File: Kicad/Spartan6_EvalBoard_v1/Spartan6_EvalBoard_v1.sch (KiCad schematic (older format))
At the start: 0 parts

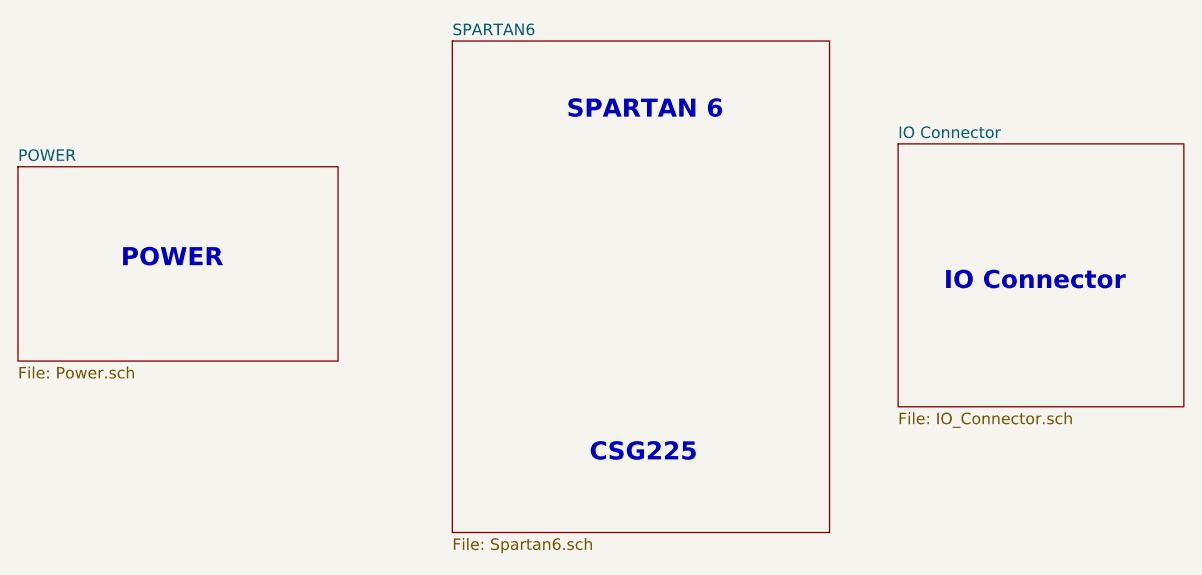
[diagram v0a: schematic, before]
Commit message: Schematic almost done
Schematic almost done, just to connect connector to FPGA
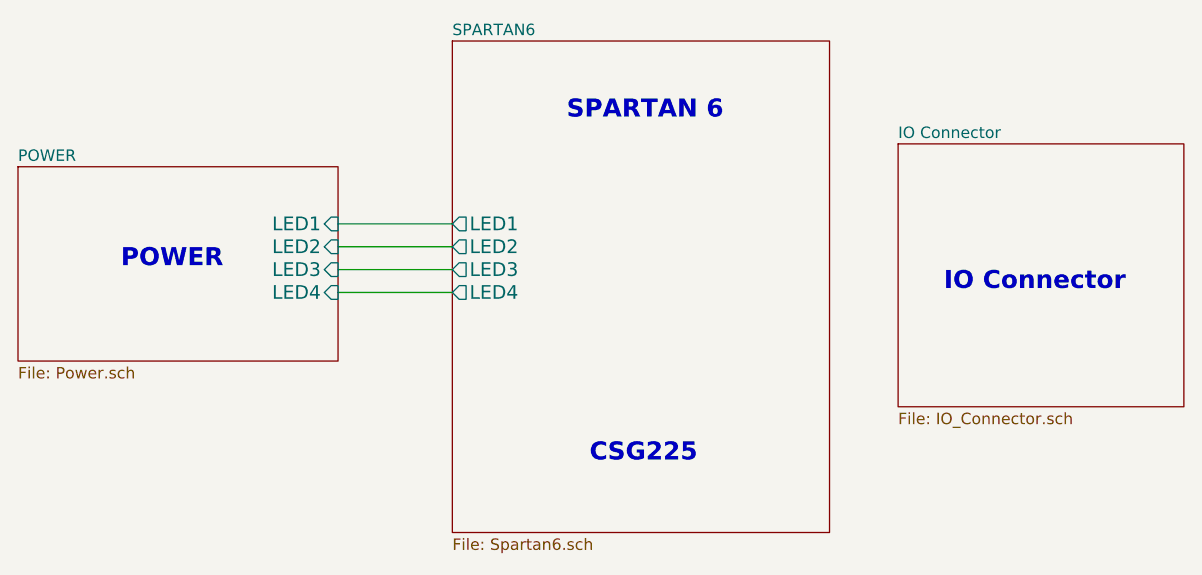
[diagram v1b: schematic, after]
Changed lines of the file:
@@
 LIBS:adc-dac
 LIBS:memory
-LIBS:xilinx
 LIBS:special
 LIBS:microcontrollers
@@
 LIBS:valves
 LIBS:numato_kicad_lib
+LIBS:xilinx
+LIBS:Eric
 LIBS:Spartan6_EvalBoard_v1-cache
 EELAYER 27 0
@@
 Sheet 1 4
 Title ""
-Date "26 sep 2014"
+Date "1 oct 2014"
 Rev ""
 Comp ""
@@
 F0 "POWER" 50
 F1 "Power.sch" 50
+F2 "LED1" I R 4500 3250 60
+F3 "LED2" I R 4500 3350 60
+F4 "LED3" I R 4500 3450 60
+F5 "LED4" I R 4500 3550 60
 $EndSheet
 Text Notes 3550 3450 0    79   ~ 16
@@
 F0 "SPARTAN6" 50
 F1 "Spartan6.sch" 50
+F2 "LED1" O L 5000 3250 60
+F3 "LED2" O L 5000 3350 60
+F4 "LED3" O L 5000 3450 60
+F5 "LED4" O L 5000 3550 60
 $EndSheet
 Text Notes 5600 4300 0    79   ~ 16
 CSG225
+Wire Wire Line
+	5000 3250 4500 3250
+Wire Wire Line
+	5000 3350 4500 3350
+Wire Wire Line
+	5000 3450 4500 3450
+Wire Wire Line
+	5000 3550 4500 3550
 $EndSCHEMATC

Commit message: Schematic and netllist created
The correct fpga connection to connector will have to be carried out.
Some more footprints need to be created.
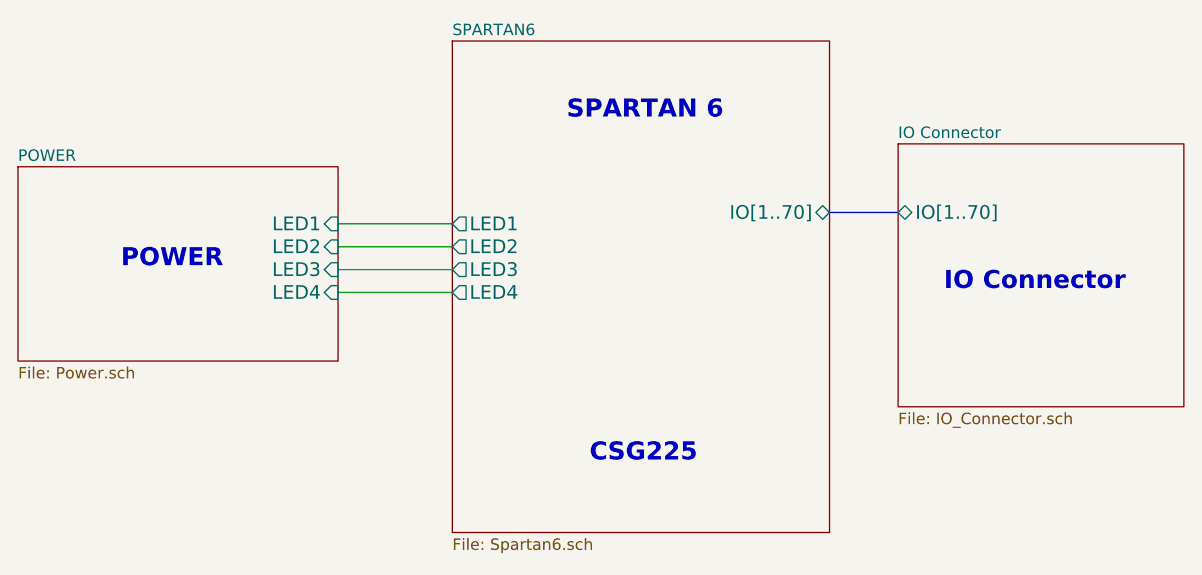
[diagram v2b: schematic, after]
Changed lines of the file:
@@
 Sheet 1 4
 Title ""
-Date "1 oct 2014"
+Date "2 oct 2014"
 Rev ""
 Comp ""
@@
 F0 "IO Connector" 50
 F1 "IO_Connector.sch" 50
+F2 "IO[1..70]" B L 6950 3200 60
 $EndSheet
 Text Notes 7150 3550 0    79   ~ 16
@@
 F4 "LED3" O L 5000 3450 60
 F5 "LED4" O L 5000 3550 60
+F6 "IO[1..70]" B R 6650 3200 60
 $EndSheet
 Text Notes 5600 4300 0    79   ~ 16
@@
 Wire Wire Line
 	5000 3550 4500 3550
+Wire Bus Line
+	6950 3200 6650 3200
 $EndSCHEMATC

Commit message: Schematic completed, layout starte
Schematic completed, layout starte
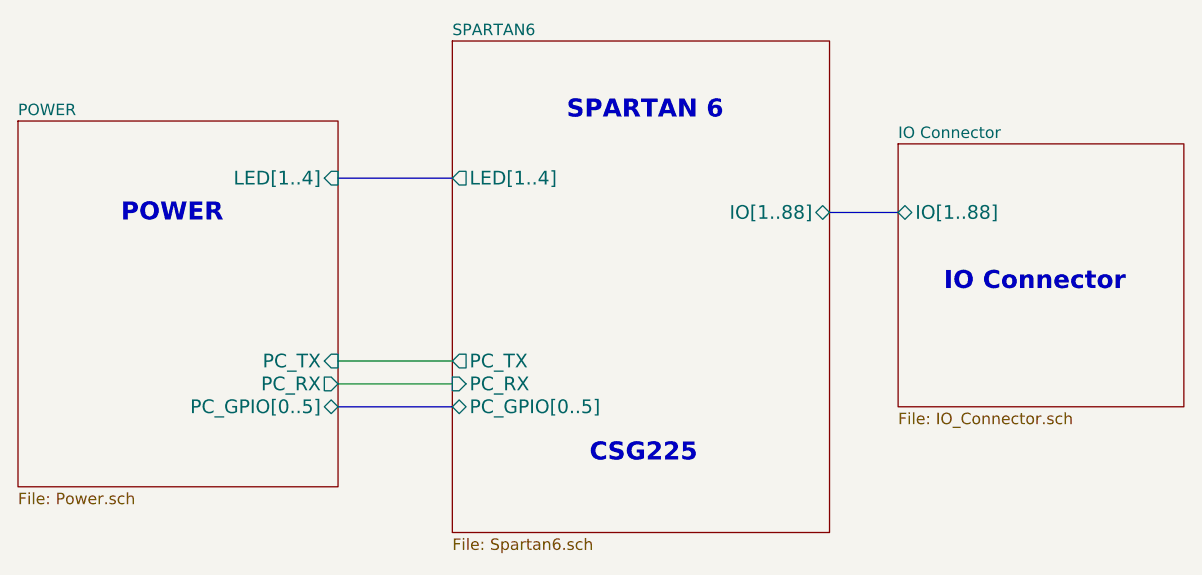
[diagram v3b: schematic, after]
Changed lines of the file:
@@
 Sheet 1 4
 Title ""
-Date "2 oct 2014"
+Date "22 oct 2014"
 Rev ""
 Comp ""
@@
 F0 "IO Connector" 50
 F1 "IO_Connector.sch" 50
-F2 "IO[1..70]" B L 6950 3200 60
+F2 "IO[1..88]" B L 6950 3200 60
 $EndSheet
 Text Notes 7150 3550 0    79   ~ 16
 IO Connector
+Text Notes 3550 3250 0    79   ~ 16
+POWER
+Text Notes 5600 4300 0    79   ~ 16
+CSG225
 $Sheet
-S 3100 3000 1400 850
+S 3100 2800 1400 1600
 U 5425C5A1
 F0 "POWER" 50
 F1 "Power.sch" 50
-F2 "LED1" I R 4500 3250 60
-F3 "LED2" I R 4500 3350 60
-F4 "LED3" I R 4500 3450 60
-F5 "LED4" I R 4500 3550 60
+F2 "LED[1..4]" I R 4500 3050 60
+F3 "PC_GPIO[0..5]" B R 4500 4050 60
+F4 "PC_TX" I R 4500 3850 60
+F5 "PC_RX" O R 4500 3950 60
 $EndSheet
-Text Notes 3550 3450 0    79   ~ 16
-POWER
+Wire Bus Line
+	6950 3200 6650 3200
+Wire Wire Line
+	5000 3850 4500 3850
+Wire Wire Line
+	4500 3950 5000 3950
+Wire Bus Line
+	4500 4050 5000 4050
 $Sheet
 S 5000 2450 1650 2150
@@
 F0 "SPARTAN6" 50
 F1 "Spartan6.sch" 50
-F2 "LED1" O L 5000 3250 60
-F3 "LED2" O L 5000 3350 60
-F4 "LED3" O L 5000 3450 60
-F5 "LED4" O L 5000 3550 60
-F6 "IO[1..70]" B R 6650 3200 60
+F2 "LED[1..4]" O L 5000 3050 60
+F3 "IO[1..88]" B R 6650 3200 60
+F4 "PC_GPIO[0..5]" B L 5000 4050 60
+F5 "PC_TX" O L 5000 3850 60
+F6 "PC_RX" I L 5000 3950 60
 $EndSheet
-Text Notes 5600 4300 0    79   ~ 16
-CSG225
-Wire Wire Line
-	5000 3250 4500 3250
-Wire Wire Line
-	5000 3350 4500 3350
-Wire Wire Line
-	5000 3450 4500 3450
-Wire Wire Line
-	5000 3550 4500 3550
 Wire Bus Line
-	6950 3200 6650 3200
+	5000 3050 4500 3050
 $EndSCHEMATC

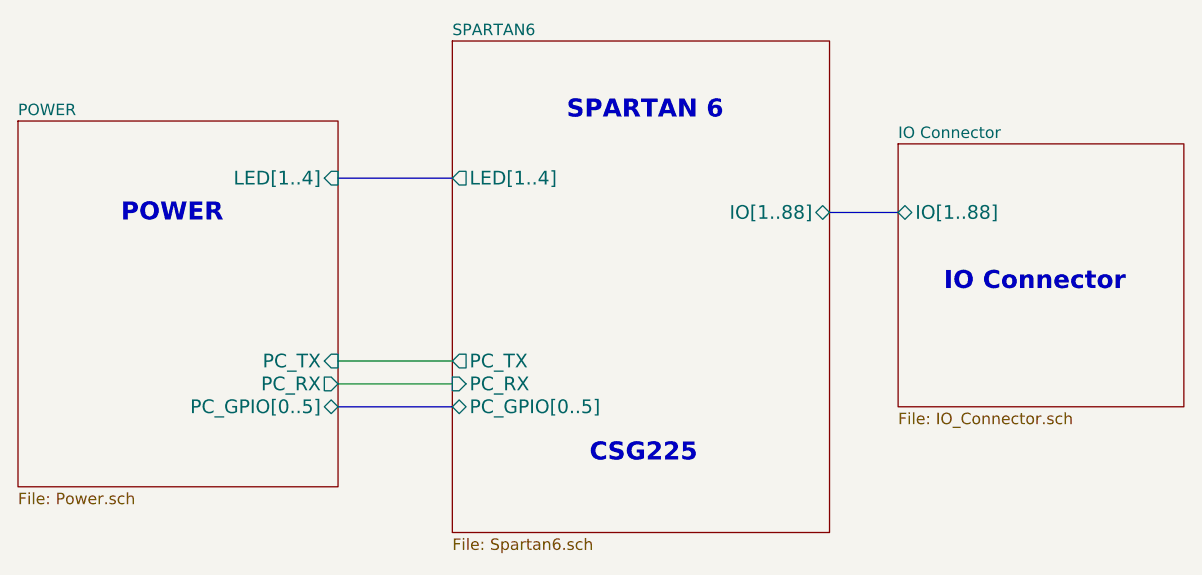
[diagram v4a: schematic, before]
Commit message: Layout completed, just need to run DRC.
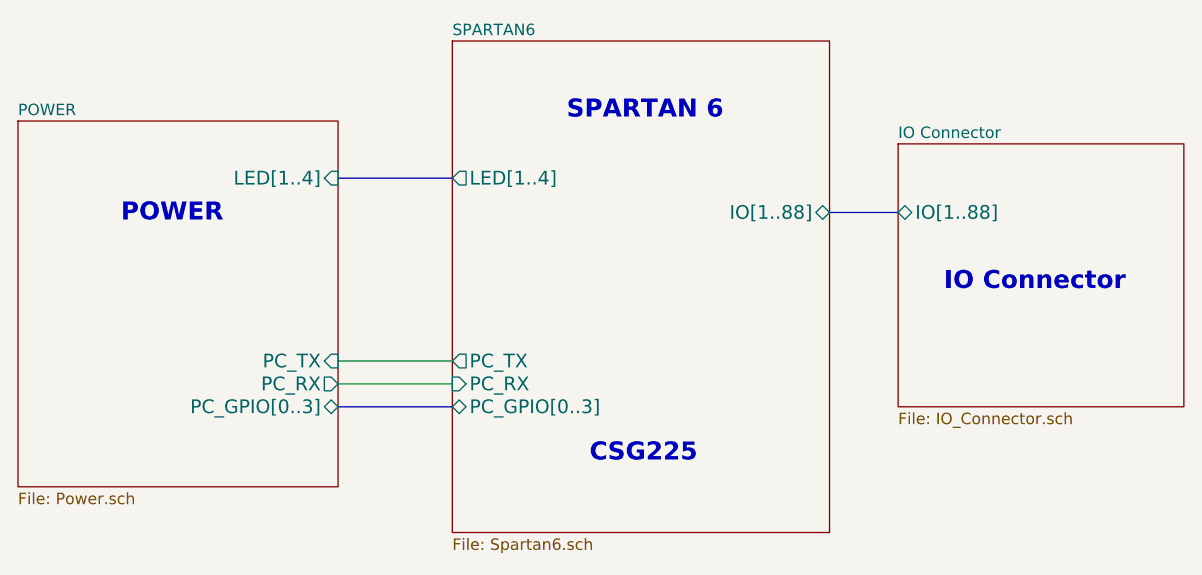
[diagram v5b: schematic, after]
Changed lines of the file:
@@
 F1 "Power.sch" 50
 F2 "LED[1..4]" I R 4500 3050 60
-F3 "PC_GPIO[0..5]" B R 4500 4050 60
+F3 "PC_GPIO[0..3]" B R 4500 4050 60
 F4 "PC_TX" I R 4500 3850 60
 F5 "PC_RX" O R 4500 3950 60
@@
 F2 "LED[1..4]" O L 5000 3050 60
 F3 "IO[1..88]" B R 6650 3200 60
-F4 "PC_GPIO[0..5]" B L 5000 4050 60
+F4 "PC_GPIO[0..3]" B L 5000 4050 60
 F5 "PC_TX" O L 5000 3850 60
 F6 "PC_RX" I L 5000 3950 60
